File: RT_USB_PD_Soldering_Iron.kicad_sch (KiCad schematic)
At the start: 63 parts, among them J1 USB4105-GF-A, J2 35RASMT4BHNTRX, SW1 SW_Push, SW2 SW_Push, U1 SPX3819M5-L-3-3, U2 BMI270, U3 DRTR5V0U4S-7, U5 STM32G431Kxxx, U6 TPS25982ONRGET, U7 OPA376AIDCKR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

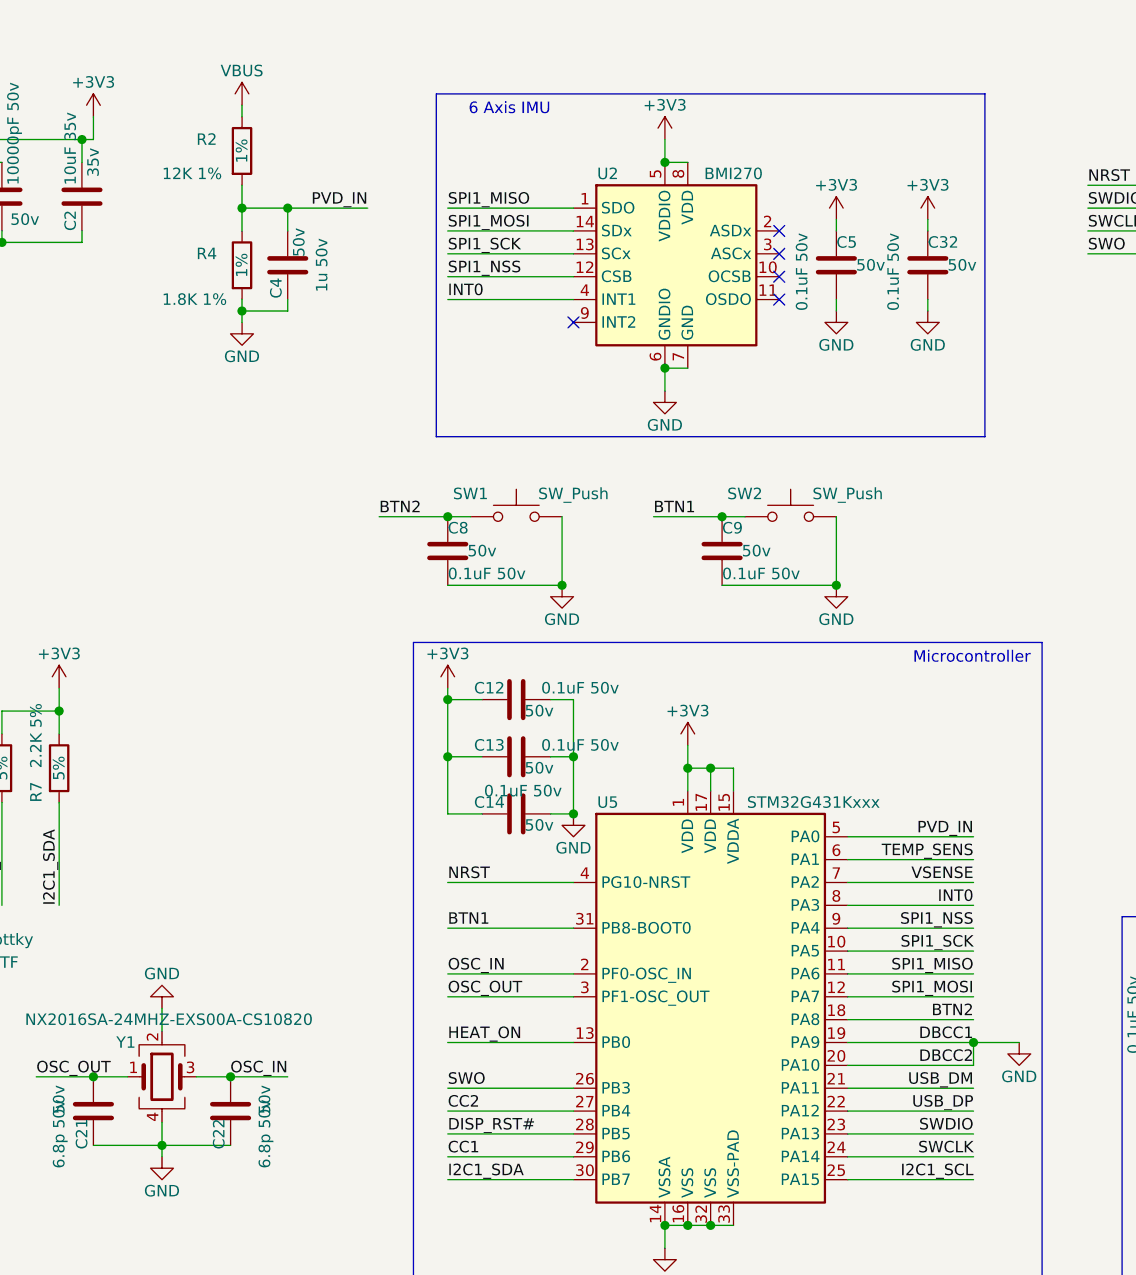
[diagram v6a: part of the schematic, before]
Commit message: redo USB traces with impedence calculations
rename usb traces and do calculations for 90 ohm impedence
also change voltage sense resistors to higher values
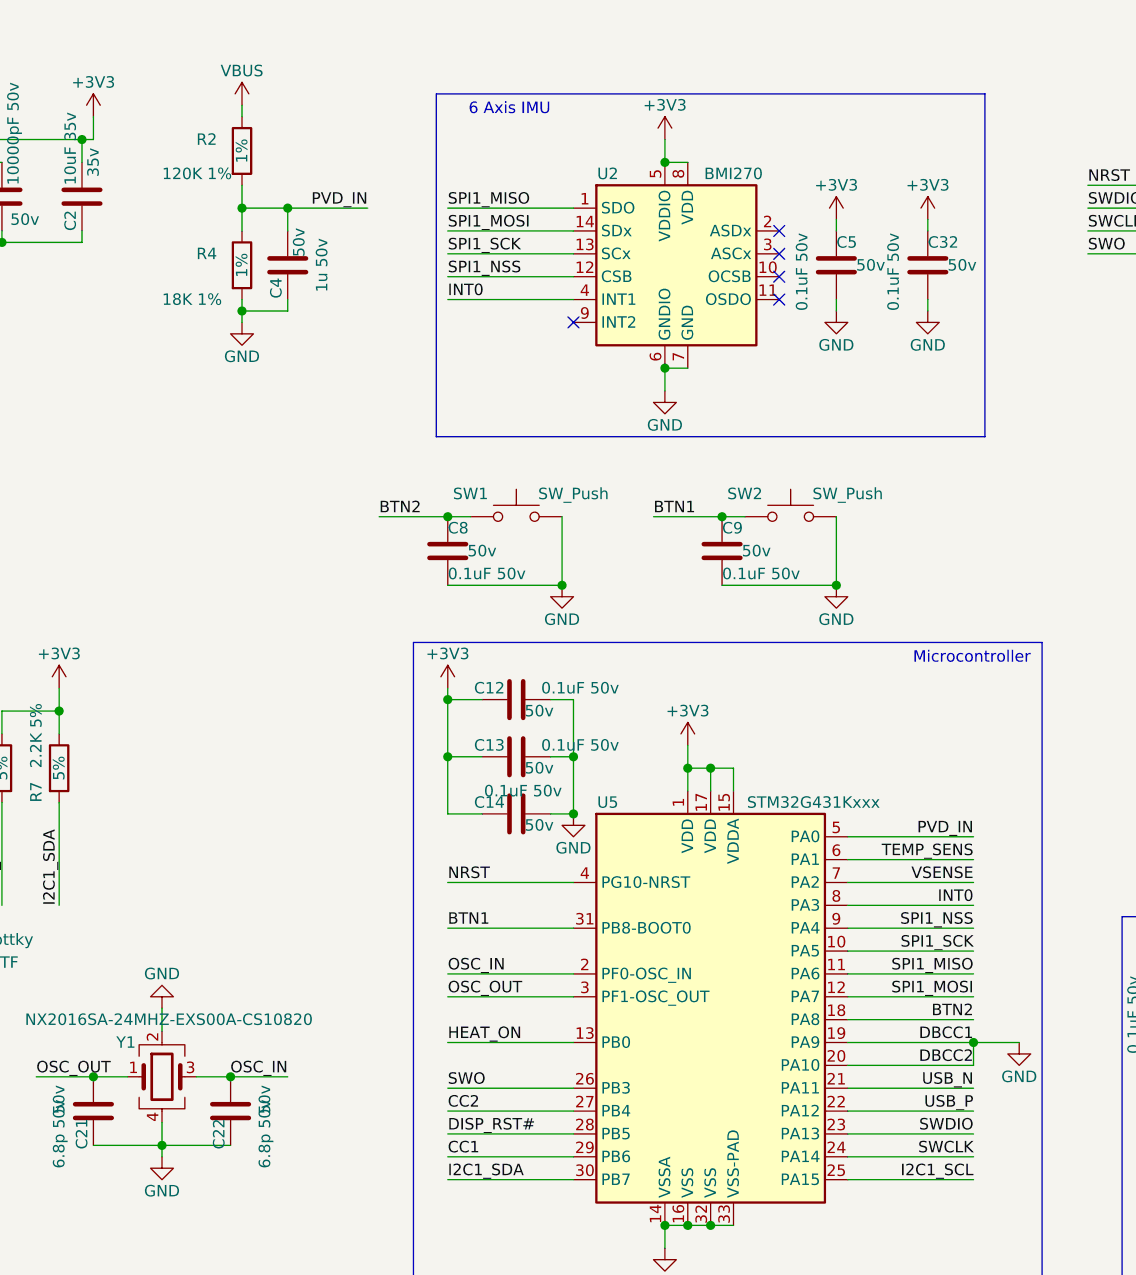
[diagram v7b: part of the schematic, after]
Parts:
- R2: value 12K 1% -> 120K 1%
- R4: value 1.8K 1% -> 18K 1%
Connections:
- net USB_DM: no longer U5.21 (PA11)
- net USB_DP: no longer U5.22 (PA12)
- new net USB_N: U5.21 (PA11)
- new net USB_P: U5.22 (PA12)
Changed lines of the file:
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@@
   (junction (at 232.41 154.94) (diameter 1.016) (color 0 0 0 0))
   (junction (at 243.84 132.08) (diameter 1.016) (color 0 0 0 0))
-  (no_connect (at 189.23 46.99))
-  (no_connect (at 189.23 44.45))
   (no_connect (at 43.18 50.8))
   (no_connect (at 43.18 53.34))
+  (no_connect (at 189.23 44.45))
   (no_connect (at 166.37 49.53))
-  (no_connect (at 147.32 176.53))
   (no_connect (at 189.23 41.91))
   (no_connect (at 189.23 39.37))
+  (no_connect (at 147.32 176.53))
+  (no_connect (at 189.23 46.99))
   (wire (pts (xy 17.78 168.91) (xy 29.21 168.91))
     (stroke (width 0) (type solid) (color 0 0 0 0))
@@
     (effects (font (size 1.27 1.27)) (justify right bottom))
   )
-  (label "USB_DM" (at 210.82 134.62 180)
-    (effects (font (size 1.27 1.27)) (justify right bottom))
-  )
-  (label "USB_DP" (at 210.82 137.16 180)
+  (label "USB_N" (at 210.82 134.62 180)
+    (effects (font (size 1.27 1.27)) (justify right bottom))
+  )
+  (label "USB_P" (at 210.82 137.16 180)
     (effects (font (size 1.27 1.27)) (justify right bottom))
   )
@@
       (effects (font (size 1.27 1.27)) (justify left))
     )
-    (property "Value" "12K 1%" (id 1) (at 120.65 33.02 0)
+    (property "Value" "120K 1%" (id 1) (at 120.65 33.02 0)
       (effects (font (size 1.27 1.27)) (justify left))
     )
@@
       (effects (font (size 1.27 1.27)) (justify left))
     )
-    (property "Value" "1.8K 1%" (id 1) (at 120.65 46.99 0)
+    (property "Value" "18K 1%" (id 1) (at 120.65 46.99 0)
       (effects (font (size 1.27 1.27)) (justify left))
     )
@@
     )
     (path "/88027881-d3dc-4c8f-8a89-19c23e8fc164"
-      (reference "R2") (unit 1) (value "12K 1%") (footprint "Resistor_SMD:R_0402_1005Metric")
+      (reference "R2") (unit 1) (value "120K 1%") (footprint "Resistor_SMD:R_0402_1005Metric")
     )
     (path "/1a2c38a0-0095-470b-8400-3a8bdde888af"
-      (reference "R4") (unit 1) (value "1.8K 1%") (footprint "Resistor_SMD:R_0402_1005Metric")
+      (reference "R4") (unit 1) (value "18K 1%") (footprint "Resistor_SMD:R_0402_1005Metric")
     )
     (path "/8fec0000-de8e-4e27-8a43-083d5fd52b1a"

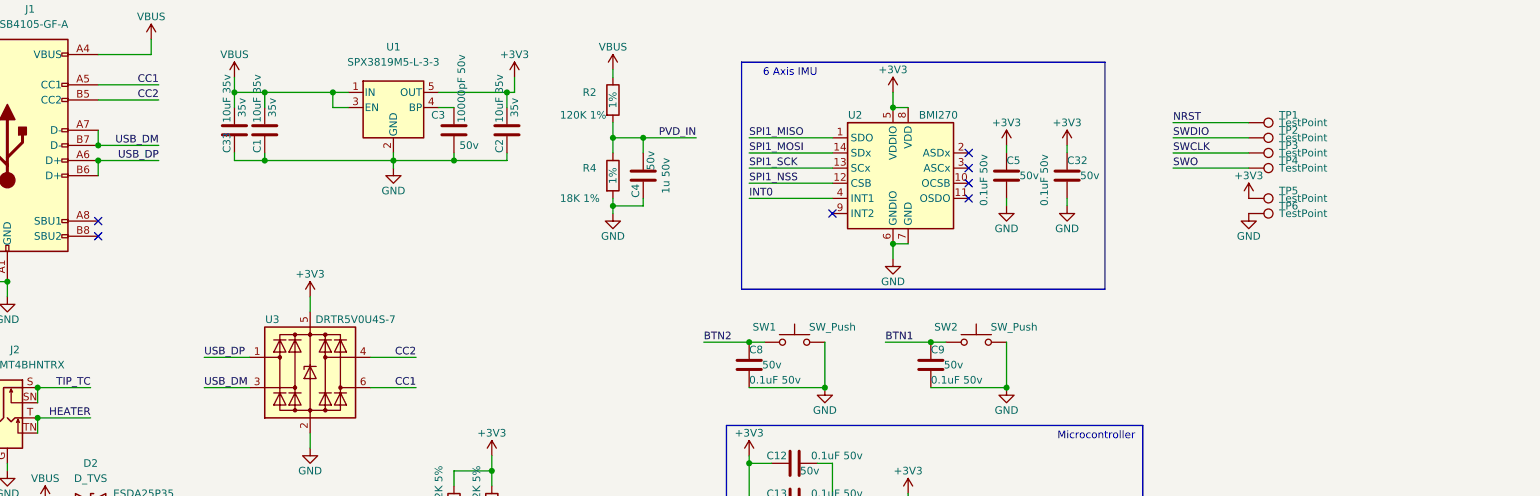
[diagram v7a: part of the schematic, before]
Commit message: remove test points and replace with connector. fix USB nets
also adjust default thermals for zone, sync pcb with schematic
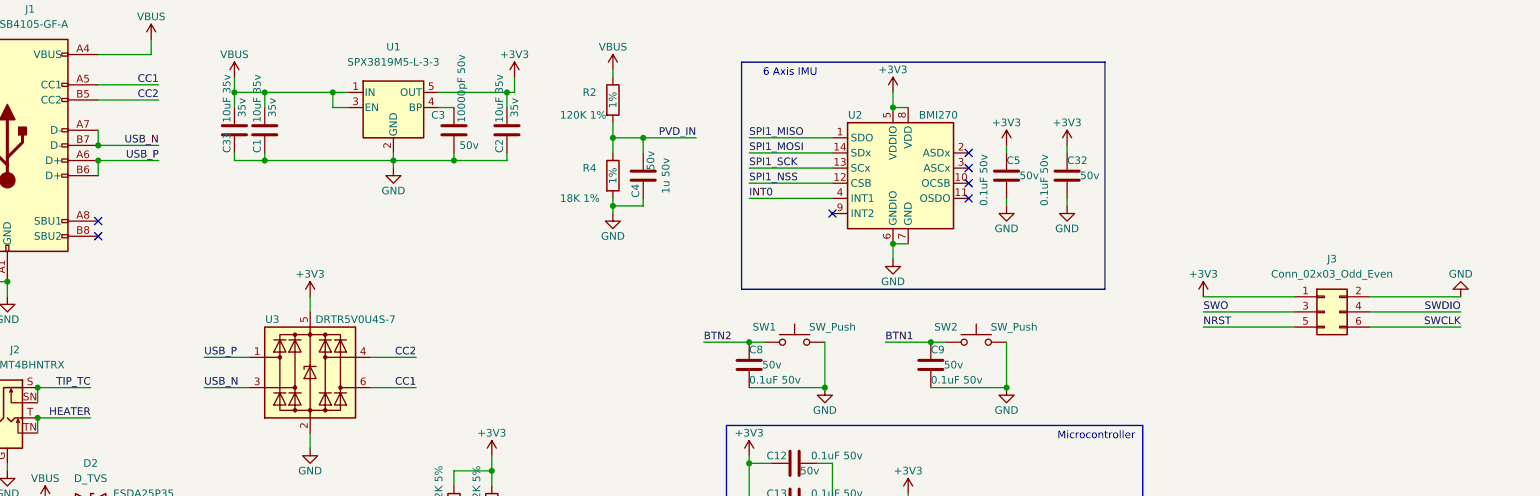
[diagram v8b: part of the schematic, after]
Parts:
- removed TP1, TP2, TP3, TP4, TP5, TP6: TestPoint, TestPoint:TestPoint_Pad_D1.0mm, symbol Connector:TestPoint
- added J3: Conn_02x03_Odd_Even, Basic_SMD:PinHeader_2x03_P1.00mm_Vertical_SMD, symbol Connector_Generic:Conn_02x03_Odd_Even
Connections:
- net USB_DM is gone; now on net USB_N: J1.A7 (D-), J1.B7 (D-), U3.3 (I/O2)
- net USB_DP is gone; now on net USB_P: J1.A6 (D+), J1.B6 (D+), U3.1 (I/O1)
- net +3V3: now also J3.1 (Pin_1)
- net GND: now also J3.2 (Pin_2)
- net NRST: now also J3.5 (Pin_5)
- net SWCLK: now also J3.6 (Pin_6)
- net SWDIO: now also J3.4 (Pin_4)
- net SWO: now also J3.3 (Pin_3)
